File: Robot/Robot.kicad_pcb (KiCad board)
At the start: 2 copper layers, 112 x 156 mm, 161 parts, among them J1 Servo1, J10 Lidar, J11 Console, J12 M1, J13 M2, J14 M3, J15 M4, J16 Battery, J17 DE9_Receptacle, J18 Balance, J2 Servo2, J3 Servo3, J4 Servo4, J5 Servo5, J6 Servo6, J7 Servo7, J8 Beacon, J9 DLED, Q1 DMP3036SSD, Q2 Si2003, SW1 User, SW2 Pwr, U1 ADC128D818, U10 SY8366HQQC, U11 SY8366HQQC, U12 SY8366HQQC, U13 INA180A2, U14 INA180A2, U15 INA180A2, U16 INA180A2, U2 MaixCAM2, U3 DRV8845RHHR, U4 ICE40UP5K-SG48ITR, U5 74HCT245, U6 MCP4728, U7 NC7SZ175, U8 TLV70212DBVR, U9 TMI6050-33

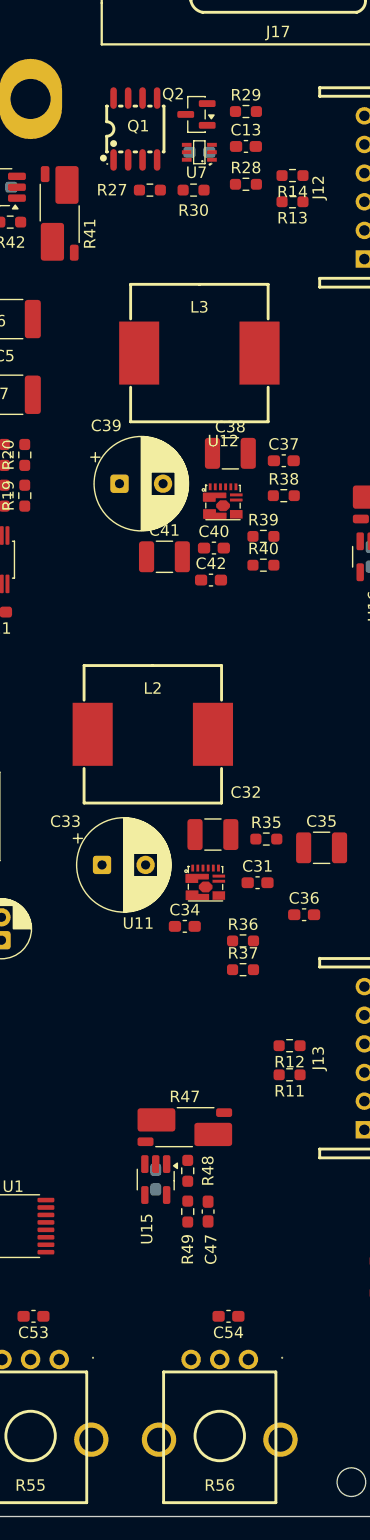
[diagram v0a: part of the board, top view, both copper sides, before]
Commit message: Updated SCH & PCB for Robot
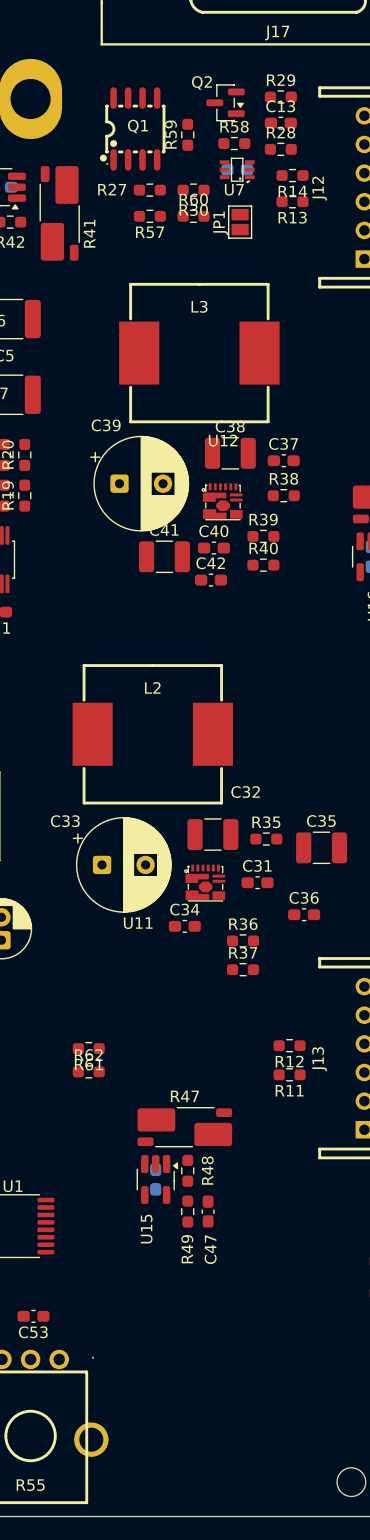
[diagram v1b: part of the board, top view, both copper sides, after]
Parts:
- removed C54: 1.0, Capacitor_SMD:C_0603_1608Metric_Pad1.08x0.95mm_HandSolder
- removed R56: RK09K1130A6S, easyeda2kicad:RES-TH_RK09K1130A6S
- added JP1: Off, Jumper:SolderJumper-2_P1.3mm_Open_Pad1.0x1.5mm, F.Cu at (145.3, 65.0)
- added R57: 100, Resistor_SMD:R_0603_1608Metric_Pad0.98x0.95mm_HandSolder, F.Cu at (137.4, 64.5)
- added R58: 100, Resistor_SMD:R_0603_1608Metric_Pad0.98x0.95mm_HandSolder, F.Cu at (144.8, 58.2)
- added R59: 100, Resistor_SMD:R_0603_1608Metric_Pad0.98x0.95mm_HandSolder, F.Cu at (140.7, 57.4)
- added R60: 1K, Resistor_SMD:R_0603_1608Metric_Pad0.98x0.95mm_HandSolder, F.Cu at (141.2, 64.5)
- added R61: R, Resistor_SMD:R_0603_1608Metric_Pad0.98x0.95mm_HandSolder, F.Cu at (132.1, 137.2)
- added R62: R, Resistor_SMD:R_0603_1608Metric_Pad0.98x0.95mm_HandSolder, F.Cu at (132.1, 139.2)
- moved R28 4.31 mm to (148.8, 58.7)
- moved C13 3.66 mm to (148.8, 56.4)
- moved C12 3.64 mm to (145.0, 60.5)
- moved U7 3.64 mm to (145.0, 60.5)
- moved R29 3.30 mm to (148.8, 54.1)
- moved Q2 2.74 mm to (144.0, 54.6)
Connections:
- C45 pad 1: /S1 -> /S5
- D4 pad 1: Net-(Q1A-G) -> Net-(D4-Pad1)
- J10 pad 5: +5V -> +3.3V
- Q2 pad 3: Net-(Q1A-G) -> Net-(Q2-D)
- R45 pad 1: /S1 -> /S5
- R46 pad 2: /S1 -> /S5
- U1 pad 9: /Pots/O3 -> Net-(U1-IN7)
- U7 pad 4: Net-(Q2-G) -> Net-(U7-Q)
- U7 pad 6: /FPGA/PWR_OFF -> Net-(JP1-B)

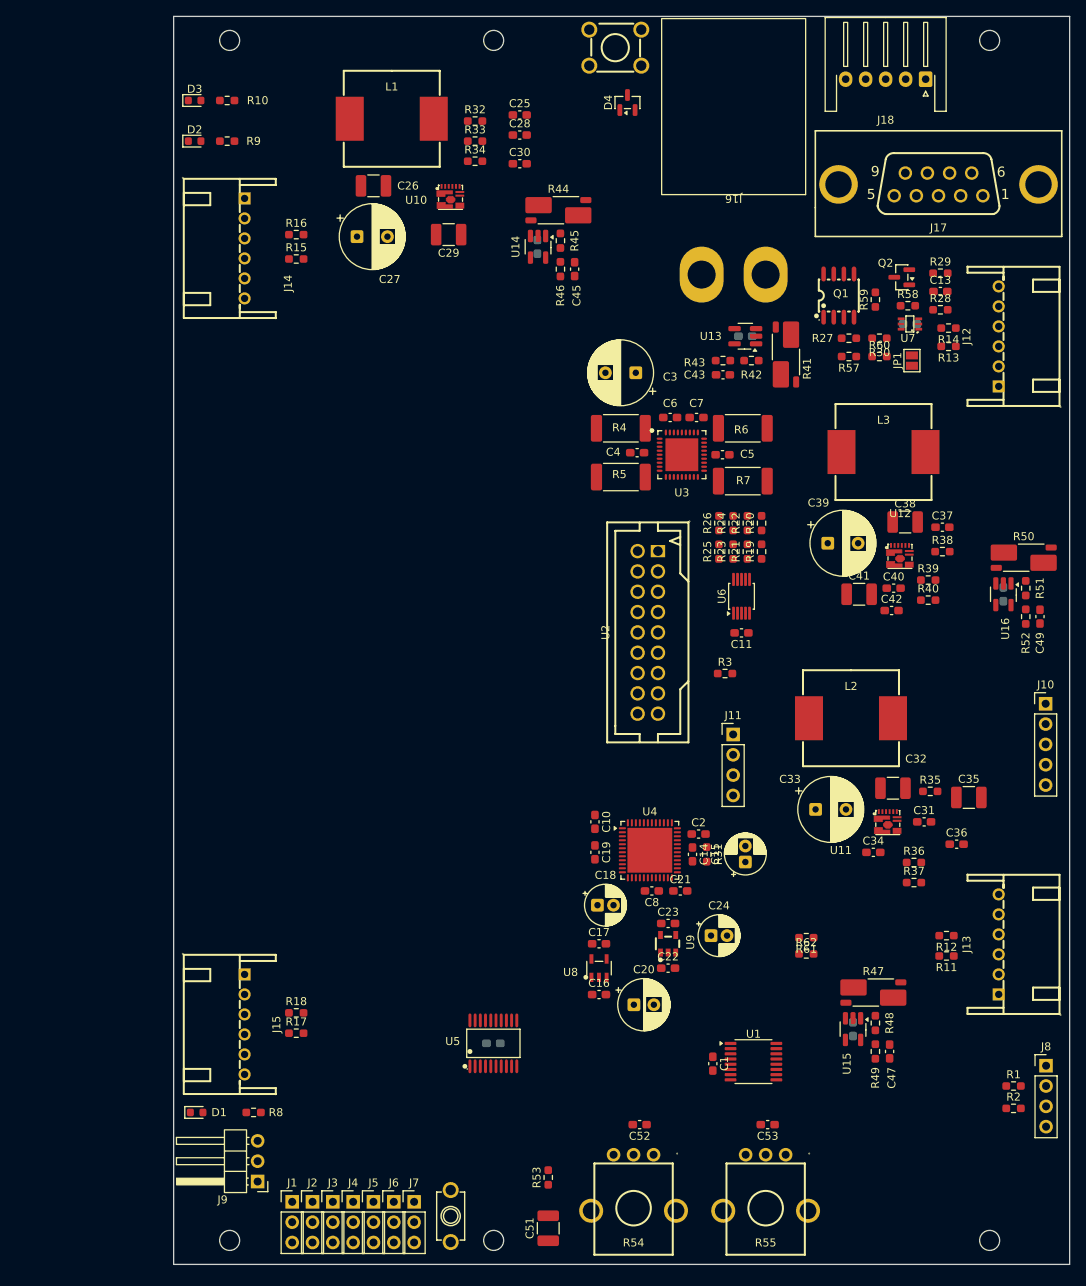
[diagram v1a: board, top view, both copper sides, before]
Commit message: Updated SCH & PCB for Robot
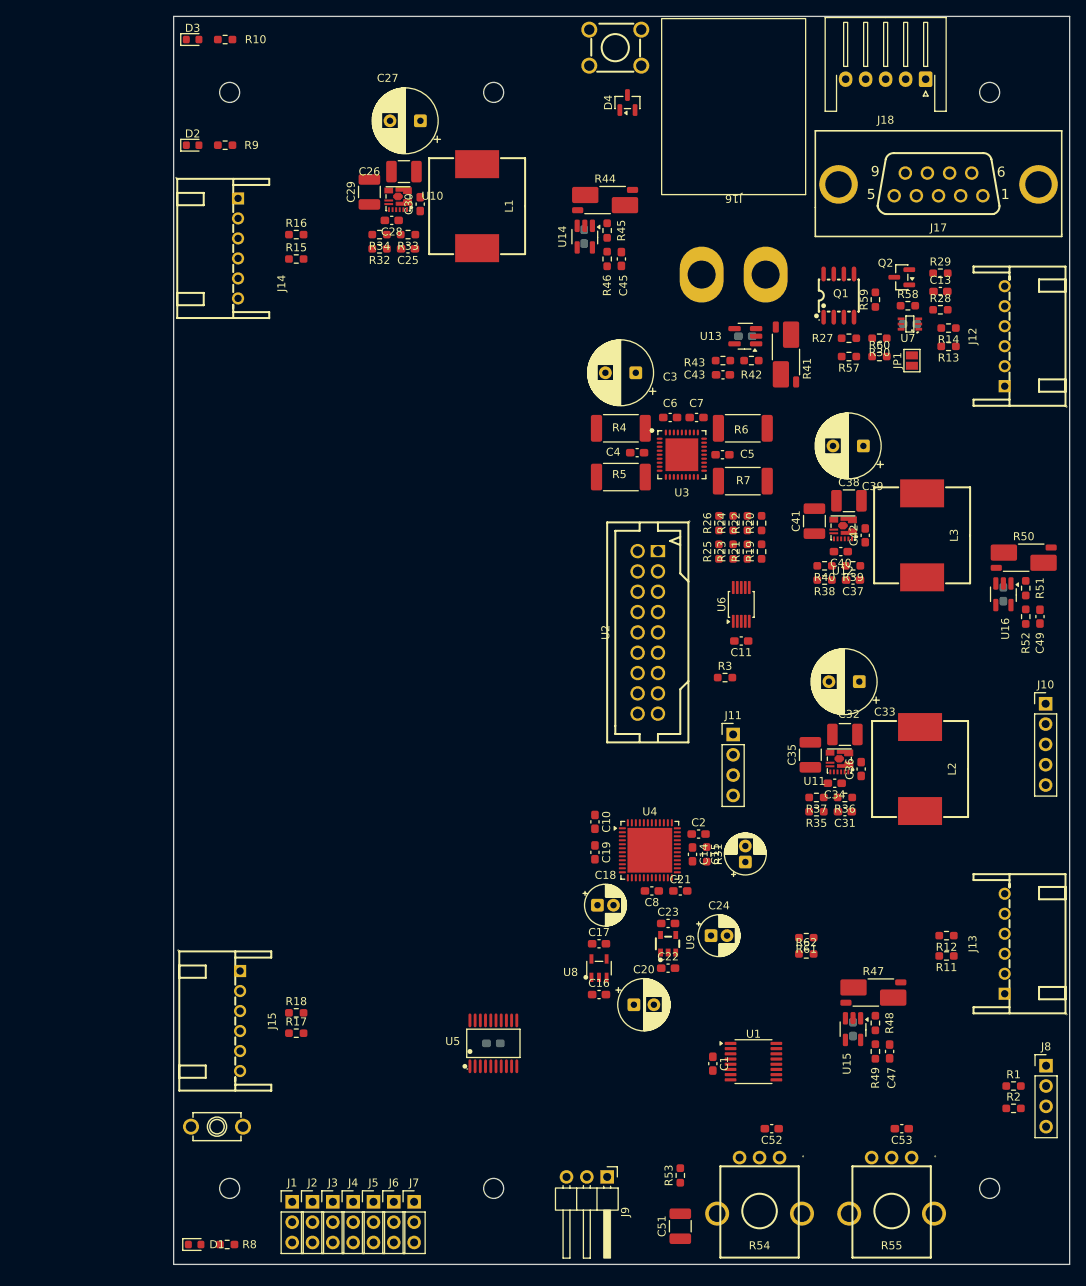
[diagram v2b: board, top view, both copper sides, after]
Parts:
- moved J9 43.7 mm to (107.2, 167.1), turned to -90 degrees
- moved SW1 31.3 mm to (58.4, 160.8), turned to 0 degrees
- moved C25 21.8 mm to (82.3, 51.1), turned to 180 degrees
- moved C35 20.5 mm to (132.6, 114.3), turned to 90 degrees
- moved R32 19.9 mm to (78.7, 51.1), turned to 180 degrees
- moved C28 19.2 mm to (80.3, 47.5), turned to 180 degrees
- moved C33 16.9 mm to (138.7, 105.2), turned to 180 degrees
- moved R8 16.8 mm to (59.7, 175.5)
- moved C53 16.8 mm to (144.0, 161.0)
- moved C52 16.5 mm to (127.8, 161.0)
- moved D1 16.5 mm to (55.6, 175.5)
- moved C51 16.5 mm to (116.3, 173.2)
- moved R53 16.5 mm to (116.3, 166.9)
- moved C27 16.5 mm to (83.8, 35.1), turned to 180 degrees
- moved R37 16.2 mm to (133.3, 119.6), turned to 180 degrees
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
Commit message: Added MaixCAM stand on SCH & PCB
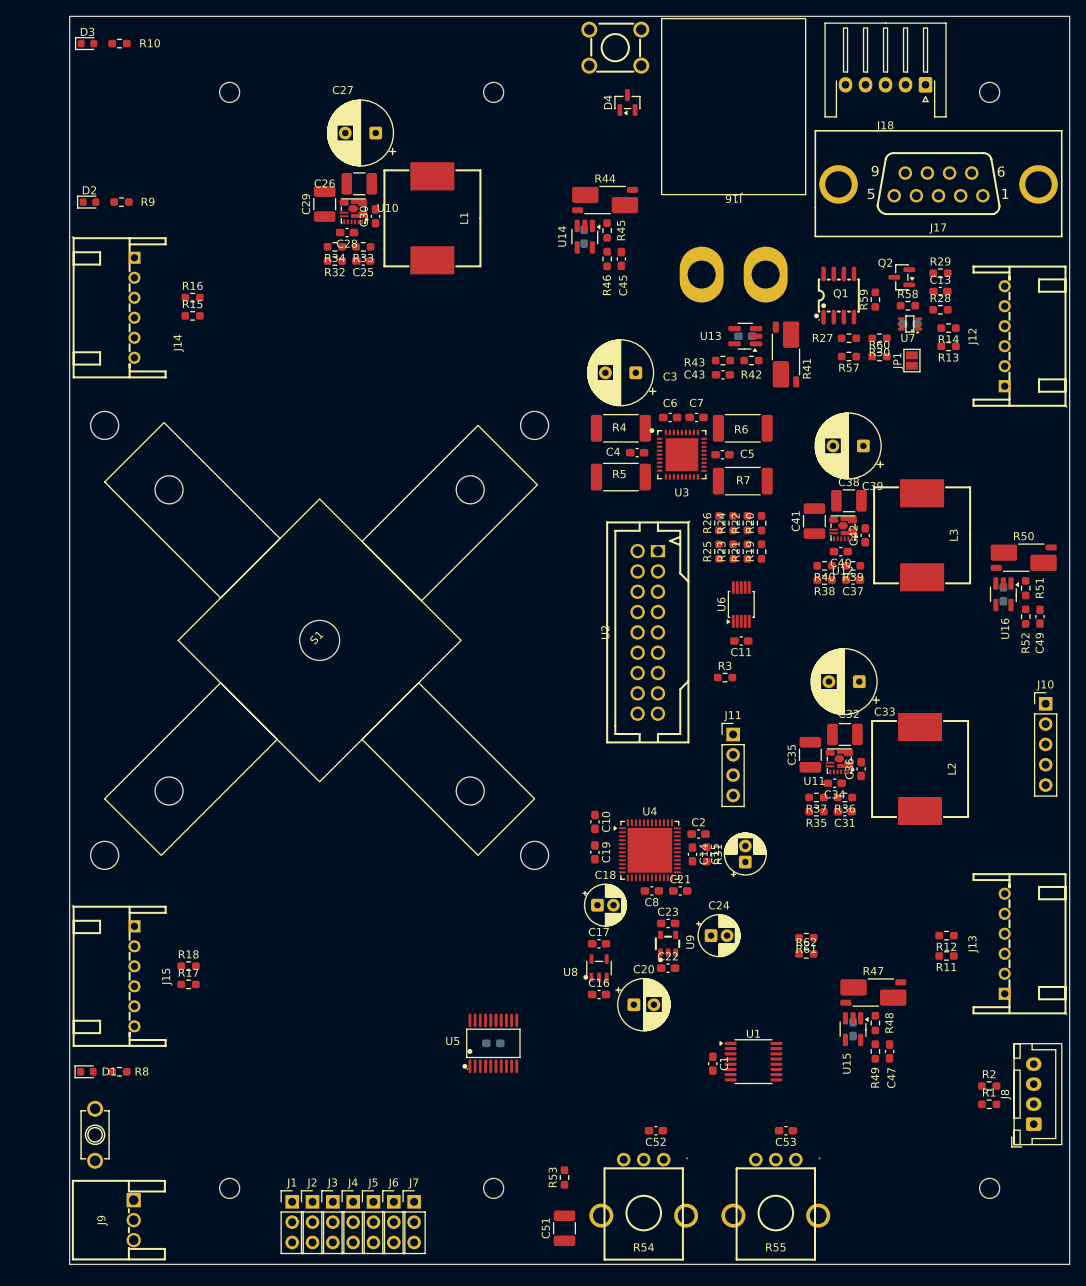
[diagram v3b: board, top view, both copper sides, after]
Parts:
- added S1: MaixCAM Stand, locals:Stand, F.Cu at (71.2, 100.0)
- J8: footprint Connector_PinHeader_2.54mm:PinHeader_1x04_P2.54mm_Vertical -> Connector_JST:JST_XH_B4B-XH-A_1x04_P2.50mm_Vertical
- J9: footprint Connector_PinHeader_2.54mm:PinHeader_1x03_P2.54mm_Horizontal -> easyeda2kicad:CONN-TH_S3B-XH-A-1-LF-SN
- moved J9 59.4 mm to (48.0, 172.5), turned to 90 degrees
- moved D1 25.4 mm to (42.2, 153.9)
- moved R8 25.4 mm to (46.2, 153.9)
- moved SW1 15.3 mm to (43.2, 161.8), turned to 90 degrees
- moved R16 15.2 mm to (55.4, 57.1)
- moved J14 14.9 mm to (48.1, 58.4)
- moved R9 14.8 mm to (46.5, 45.2)
- moved R17 14.8 mm to (54.9, 143.0)
- moved R15 14.8 mm to (55.4, 59.4)
- moved D2 14.7 mm to (42.5, 45.2)
- moved R18 14.7 mm to (54.9, 140.7)
- moved C53 14.5 mm to (129.5, 161.3)
- moved C51 14.5 mm to (101.9, 173.5)
- moved C52 14.5 mm to (113.3, 161.3)
- moved R53 14.5 mm to (101.9, 167.1)
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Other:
- board size 112 x 156 mm -> 125 x 156 mm

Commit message: Updated PCB & Patterns for Robot
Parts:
- added REF**: GRID-2_5_100, locals:GRID-2_5_100, F.Cu at (53.6, 30.5)
- added REF**: GRID-15_11_100, locals:GRID-15_11_100, F.Cu at (70.1, 50.8)
- added REF**: GRID-21_11_100, locals:GRID-21_11_100, F.Cu at (76.7, 149.9)
- added REF**: GRID-6_11_100, locals:GRID-6_11_100, F.Cu at (43.2, 40.6)
- added REF**: GRID-10_5_100, locals:GRID-10_5_100, F.Cu at (76.5, 30.5)
- R11, R12, R13, R14, R15, R16, R17, R18: moved to B.Cu
- moved C25 22.6 mm to (97.5, 61.5)
- moved C26 22.6 mm to (97.0, 51.8)
- moved C28 22.6 mm to (95.5, 57.9)
- moved C30 22.6 mm to (99.1, 55.9)
- moved L1 22.6 mm to (106.2, 56.1)
- moved R32 22.6 mm to (94.0, 61.5)
- moved R33 22.6 mm to (97.5, 59.7)
- moved R34 22.6 mm to (94.0, 59.7)
- moved U10 22.6 mm to (96.3, 55.4)
- moved C27 22.6 mm to (99.1, 45.5)
- moved C29 22.6 mm to (92.7, 54.4)
- moved C9 15.8 mm to (108.2, 154.7)
- moved U5 15.8 mm to (108.2, 154.7)
- moved R15 13.1 mm to (46.5, 69.1), turned to -90 degrees
- moved D2 12.3 mm to (37.4, 56.4)
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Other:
- board size 125 x 156 mm -> 130 x 156 mm

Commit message: Updated PCB for Robot
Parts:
- moved C47 47.5 mm to (147.6, 104.1), turned to 0 degrees
- moved D4 46.3 mm to (139.5, 68.3), turned to -90 degrees
- moved R49 46.0 mm to (147.6, 105.9), turned to 180 degrees
- moved R48 42.0 mm to (144.0, 105.9), turned to 180 degrees
- moved U15 40.5 mm to (144.8, 108.7), turned to 0 degrees
- moved C48 40.4 mm to (144.8, 108.8), turned to 180 degrees
- moved R47 31.5 mm to (145.1, 112.9)
- moved C49 26.5 mm to (148.9, 73.6), turned to 0 degrees
- moved R52 24.1 mm to (148.9, 75.4), turned to 180 degrees
- moved R51 23.0 mm to (145.4, 75.4), turned to 180 degrees
- moved U16 19.2 mm to (146.1, 78.2), turned to 0 degrees
- moved C50 19.2 mm to (146.1, 78.3), turned to 180 degrees
- moved R50 14.7 mm to (146.5, 82.3)
- moved C45 14.3 mm to (108.7, 32.2), turned to 0 degrees
- moved R46 12.6 mm to (108.7, 34.0), turned to 180 degrees
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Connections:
- D4 pad 1: Net-(D4-Pad1) -> /FPGA/PwrBtnInput
- D4 pad 2: /FPGA/PwrBtnInput -> Net-(D4-Pad2)
- J16 pad 1: GND -> Net-(J16-Pin_1)
- J16 pad 2: Net-(J16-Pin_2) -> GND
- J17 pad 1: Net-(J16-Pin_2) -> Net-(J16-Pin_1)
- J17 pad 6: Net-(J16-Pin_2) -> Net-(J16-Pin_1)
- Q1 pad 5: /Power/CSense/+ -> Net-(J16-Pin_1)
- Q1 pad 6: /Power/CSense/+ -> Net-(J16-Pin_1)
- Q1 pad 7: Net-(J16-Pin_2) -> /Power/CSense/+
- Q1 pad 8: Net-(J16-Pin_2) -> /Power/CSense/+
- R57 pad 2: Net-(D4-Pad1) -> Net-(D4-Pad2)
- U10 pad 3: unconnected-(U10-NC-Pad3) -> GND
- U10 pad 4: unconnected-(U10-NC-Pad4) -> GND
- U11 pad 3: unconnected-(U11-NC-Pad3) -> GND
- U11 pad 4: unconnected-(U11-NC-Pad4) -> GND
- U12 pad 3: unconnected-(U12-NC-Pad3) -> GND
- U12 pad 4: unconnected-(U12-NC-Pad4) -> GND
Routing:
- net GND: track 0.00 -> 104.4 mm, vias 0 -> 76
- net /Power/5VRegulator/Out: track 0.00 -> 73.5 mm
- net /Power/5VRegulator1/Out: track 0.00 -> 71.3 mm
- net /Power/5VRegulator2/Out: track 0.00 -> 70.1 mm
- net Net-(J16-Pin_1): track 0.00 -> 40.8 mm
- net +5V: track 0.00 -> 27.3 mm, vias 0 -> 4
- net +3.3V: track 0.00 -> 22.0 mm, vias 0 -> 2
- net +12V: track 0.00 -> 21.8 mm, vias 0 -> 6
- net /FPGA/PwrBtnInput: track 0.00 -> 19.2 mm
- net Net-(U13-+): track 0.00 -> 16.4 mm
- net /Power/CSense/+: track 0.00 -> 15.2 mm
- net Net-(U12-LX): track 0.00 -> 12.6 mm
- net Net-(U10-LX): track 0.00 -> 12.6 mm
- net Net-(U11-LX): track 0.00 -> 12.6 mm
- net Net-(Q1A-G): track 0.00 -> 11.6 mm
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- added copper zone on B.Cu, net GND
- added copper zone on F.Cu, net GND

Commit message: Updated PCB for Robot (routing in progress)
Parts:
- moved J14 113.7 mm to (156.9, 61.5), turned to 90 degrees
- moved J12 113.7 mm to (43.3, 66.6), turned to -90 degrees
- moved J15 113.6 mm to (156.9, 140.2), turned to 90 degrees
- moved J13 113.6 mm to (43.3, 140.2), turned to -90 degrees
- moved R15 107.6 mm to (153.7, 59.4), turned to 90 degrees
- moved R14 107.5 mm to (46.5, 68.6), turned to -90 degrees
- moved R18 107.4 mm to (153.7, 142.7), turned to -90 degrees
- moved R12 107.4 mm to (46.5, 142.5), turned to -90 degrees
- moved R11 107.2 mm to (46.5, 137.9), turned to 90 degrees
- moved R17 107.2 mm to (153.7, 138.2), turned to 90 degrees
- moved R13 107.2 mm to (46.5, 64.3), turned to 90 degrees
- moved R16 107.2 mm to (153.7, 64.0), turned to -90 degrees
- moved C1 65.3 mm to (134.6, 89.2)
- moved U1 65.3 mm to (139.7, 88.9)
- moved R62 48.6 mm to (146.3, 92.7)
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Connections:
- D1 pad 2: Net-(D1-A) -> +3.3V
- D2 pad 2: Net-(D2-A) -> +3.3V
- D3 pad 2: Net-(D3-A) -> +3.3V
- J4 pad 2: /Power/Pwr1 -> /Power/Pwr2
- J9 pad 1: /Power/Pwr2 -> /Power/Pwr1
- R10 pad 1: +3.3V -> Net-(D3-K)
- R10 pad 2: Net-(D3-A) -> Net-(U4A-RGB2)
- R8 pad 1: +3.3V -> Net-(D1-K)
- R8 pad 2: Net-(D1-A) -> Net-(U4A-RGB0)
- R9 pad 1: +3.3V -> Net-(D2-K)
- R9 pad 2: Net-(D2-A) -> Net-(U4A-RGB1)
- U4 pad 39: Net-(D1-K) -> Net-(U4A-RGB0)
- U4 pad 40: Net-(D2-K) -> Net-(U4A-RGB1)
- U4 pad 41: Net-(D3-K) -> Net-(U4A-RGB2)
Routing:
- net +3.3V: track 22.0 -> 287.6 mm
- net Net-(U4A-RGB2): track 0.00 -> 145.3 mm, vias 0 -> 1
- net Net-(J13B-M+): track 0.00 -> 126.6 mm
- net Net-(U4A-RGB1): track 0.00 -> 115.6 mm, vias 0 -> 1
- net Net-(J13B-M-): track 0.00 -> 115.0 mm
- net Net-(J12A-C1): track 0.00 -> 112.5 mm, vias 0 -> 1
- net Net-(J12A-C2): track 0.00 -> 112.5 mm, vias 0 -> 1
- net Net-(J15B-M-): track 0.00 -> 102.5 mm
- net Net-(J12B-M-): track 0.00 -> 94.9 mm
- net Net-(J15B-M+): track 0.00 -> 88.2 mm
- net /FPGA/DLED: track 0.00 -> 80.0 mm
- net Net-(J12B-M+): track 0.00 -> 79.1 mm
- net +12V: track 21.8 -> 97.9 mm, vias 6 -> 8
- net /Power/Pwr1: track 0.00 -> 70.0 mm
- net Net-(U4B-IOB_25b_G3): track 0.00 -> 68.8 mm
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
